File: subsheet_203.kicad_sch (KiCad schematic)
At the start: 14 parts, among them U203 MC68901_DIP_48_PHY, U209 74LS86_PHY, U211 74LS04_PHY, U900 74LS164_PHY, Y200 2.4576 MHz

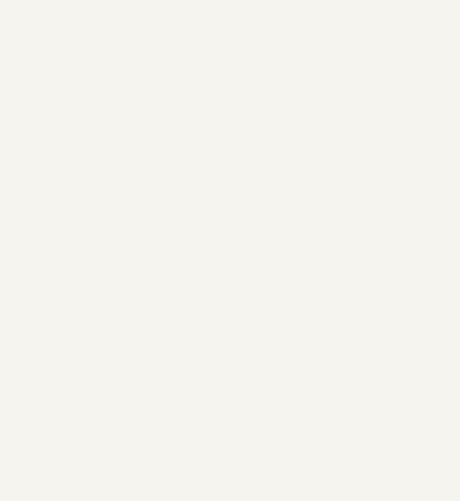
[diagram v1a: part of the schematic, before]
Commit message: add gnd/vcc symbol to start replacing local labels
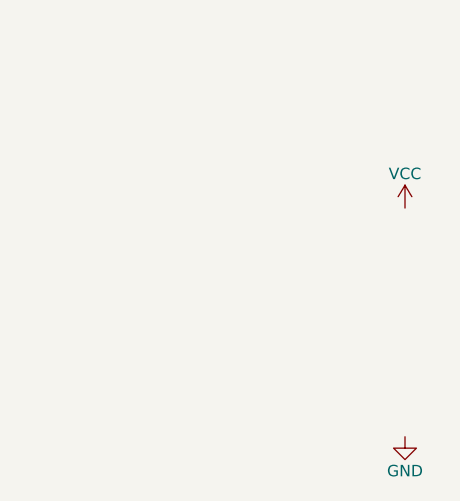
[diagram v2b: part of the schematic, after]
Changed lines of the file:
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@@
     (pin "2")
   )
+  (symbol (lib_id "power:VCC") (at 184.15 208.28 0) (unit 1)
+    (in_bom yes) (on_board yes)
+    (property "Reference" "#PWR?" (id 0) (at 184.15 212.09 0)
+      (effects (font (size 1.27 1.27)) hide)
+    )
+    (property "Value" "VCC" (id 1) (at 184.15 204.47 0))
+    (property "Footprint" "" (id 2) (at 184.15 208.28 0)
+      (effects (font (size 1.27 1.27)) hide)
+    )
+    (property "Datasheet" "" (id 3) (at 184.15 208.28 0)
+      (effects (font (size 1.27 1.27)) hide)
+    )
+    (pin "1")
+  )
+  (symbol (lib_id "power:GND") (at 184.15 233.68 0) (unit 1)
+    (in_bom yes) (on_board yes)
+    (property "Reference" "#PWR?" (id 0) (at 184.15 240.03 0)
+      (effects (font (size 1.27 1.27)) hide)
+    )
+    (property "Value" "GND" (id 1) (at 184.15 237.49 0))
+    (property "Footprint" "" (id 2) (at 184.15 233.68 0)
+      (effects (font (size 1.27 1.27)) hide)
+    )
+    (property "Datasheet" "" (id 3) (at 184.15 233.68 0)
+      (effects (font (size 1.27 1.27)) hide)
+    )
+    (pin "1")
+  )
 )
